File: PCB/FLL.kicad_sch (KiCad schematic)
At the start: 10 parts, among them J1 Jack-DC, U1 MCP73831-2-MC, U3 LM317L_SOT-89

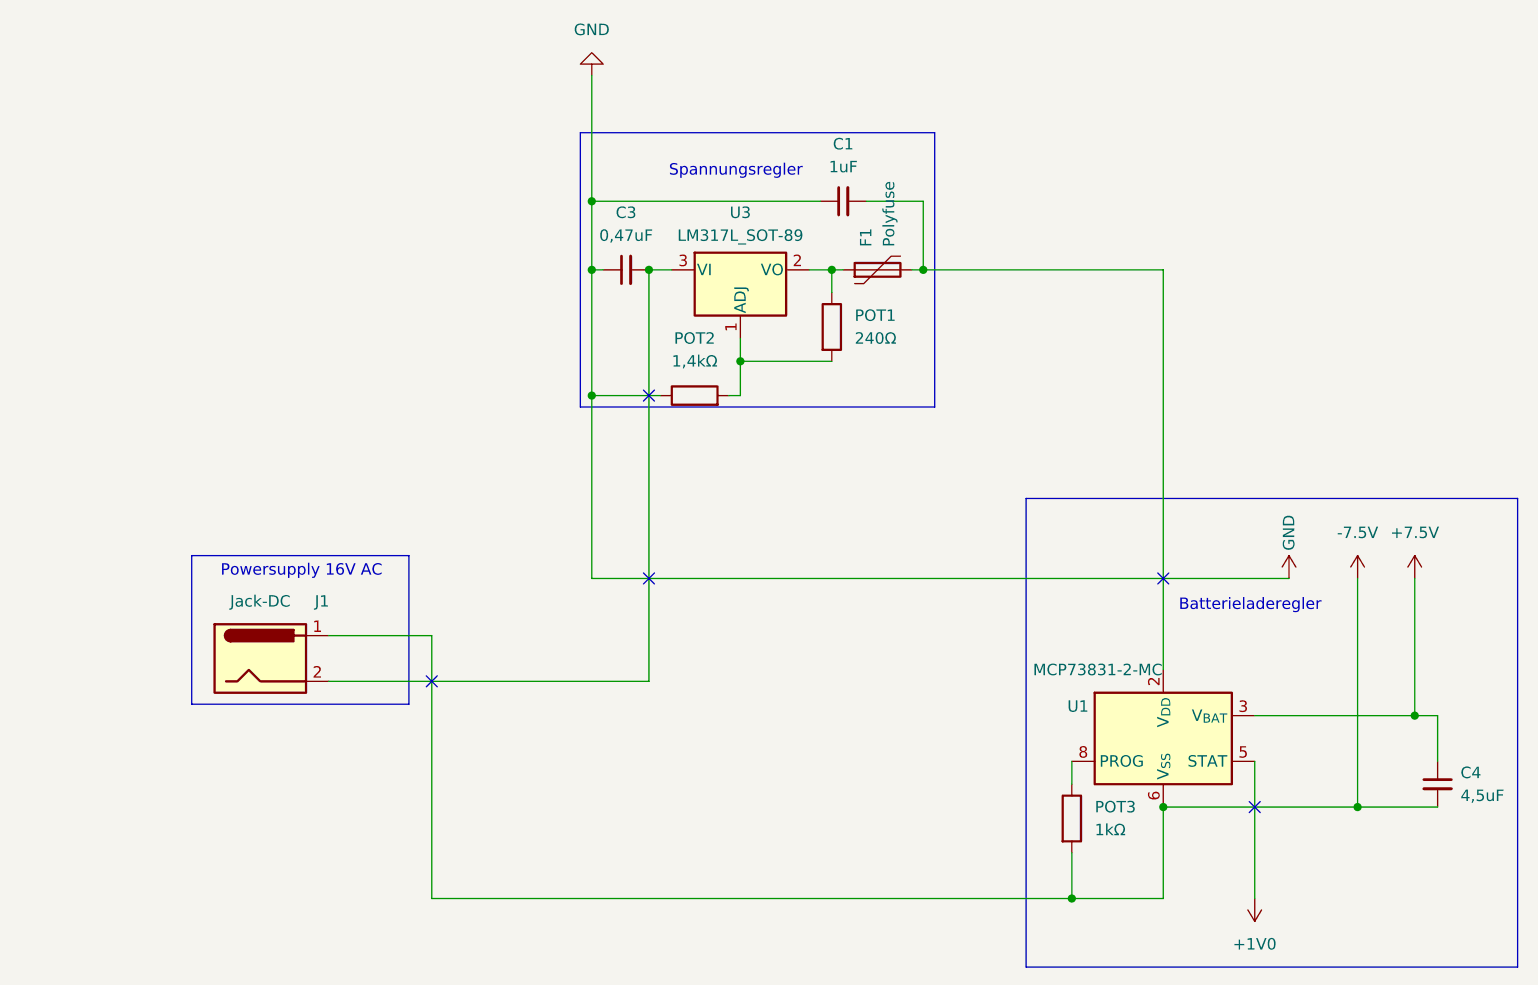
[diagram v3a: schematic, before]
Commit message: Update PCB design configuration and remove unnecessary files
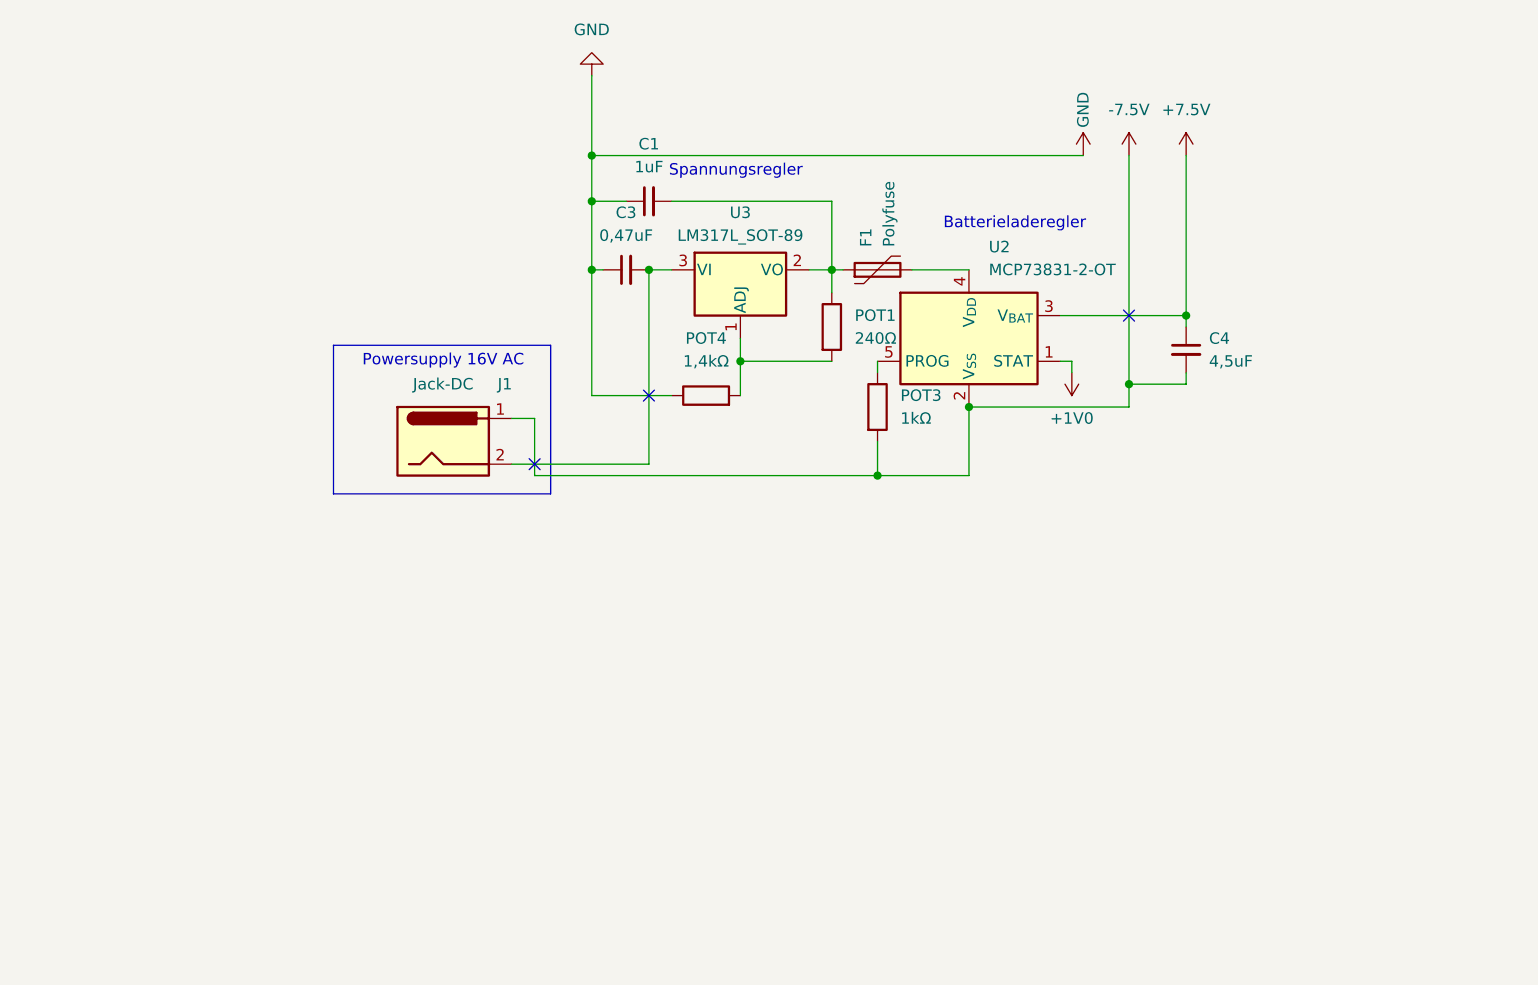
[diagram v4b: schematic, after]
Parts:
- removed POT2: 1,4kΩ, Resistor_SMD:R_0603_1608Metric_Pad0.98x0.95mm_HandSolder, symbol Device:R
- removed U1: MCP73831-2-MC, Package_DFN_QFN:DFN-8-1EP_3x2mm_P0.5mm_EP1.7x1.4mm, symbol Battery_Management:MCP73831-2-MC
- added POT4: 1,4kΩ, Resistor_SMD:R_0603_1608Metric_Pad0.98x0.95mm_HandSolder, symbol Device:R
- added U2: MCP73831-2-OT, Package_TO_SOT_SMD:SOT-23-5, symbol Battery_Management:MCP73831-2-OT
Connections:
- net +1V0: now also U2.1 (STAT)
- net +7.5V: now also U2.3 (V_{BAT})
- net -7.5V: now also U2.2 (V_{SS})
- net GND: now also POT4.1
- net at F1.1, POT1.1, U3.2 (VO): now also C1.2
- net at F1.2: now also U2.4 (V_{DD}); no longer C1.2
- net at POT1.2, U3.1 (ADJ): now also POT4.2
- net at POT3.1: now also U2.5 (PROG)
- no-connect marks 5 -> 3
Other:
- moved on the sheet: C1, C4, J1, POT3

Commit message: Added Mouser Electronics Parts
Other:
- title: Large Hub Battery LEGO: 45610 | Charger -> LEGO® Technic (TM) Large Hub Battery: 45610 | Charger
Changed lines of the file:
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@@
 	(paper "A4")
 	(title_block
-		(title "Large Hub Battery LEGO: 45610 | Charger")
+		(title "LEGO® Technic (TM) Large Hub Battery: 45610 | Charger")
 		(date "04.07.2024")
 		(rev "AIIrondev")

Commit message: chore: Remove unused KiCad symbol files
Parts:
- C1: footprint Capacitor_THT:CP_Axial_L10.0mm_D4.5mm_P15.00mm_Horizontal -> C0805C105K4RACTU:C0805
- C3: footprint Capacitor_THT:CP_Axial_L10.0mm_D4.5mm_P15.00mm_Horizontal -> C0805C474K5RACTU:C0805
- C4: value 4,5uF -> 4,7uF; footprint Capacitor_THT:CP_Axial_L10.0mm_D4.5mm_P15.00mm_Horizontal -> C1210C475K4PACTU:C1210
- POT1: value 240Ω -> 1206L05015YR; footprint Resistor_SMD:R_0603_1608Metric_Pad0.98x0.95mm_HandSolder -> 1206L075THYR:1206L05015YR
- POT3, POT4: footprint Resistor_SMD:R_0603_1608Metric_Pad0.98x0.95mm_HandSolder -> ERJ-2RHD1401X:ERJ2RKD1004X
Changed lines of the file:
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@@
 			)
 		)
-		(property "Footprint" "Capacitor_THT:CP_Axial_L10.0mm_D4.5mm_P15.00mm_Horizontal"
+		(property "Footprint" "C0805C474K5RACTU:C0805"
 			(at 119.38 83.82 0)
 			(effects
@@
 			)
 		)
-		(property "Value" "240Ω"
+		(property "Value" "1206L05015YR"
 			(at 144.78 91.4399 0)
 			(effects
@@
 			)
 		)
-		(property "Footprint" "Resistor_SMD:R_0603_1608Metric_Pad0.98x0.95mm_HandSolder"
+		(property "Footprint" "1206L075THYR:1206L05015YR"
 			(at 140.462 90.17 90)
 			(effects
@@
 			)
 		)
-		(property "Footprint" "Resistor_SMD:R_0603_1608Metric_Pad0.98x0.95mm_HandSolder"
+		(property "Footprint" "ERJ-2RHD1401X:ERJ2RKD1004X"
 			(at 145.542 99.06 90)
 			(effects
@@
 			)
 		)
-		(property "Value" "4,5uF"
+		(property "Value" "4,7uF"
 			(at 184.15 93.9862 0)
 			(effects
@@
 			)
 		)
-		(property "Footprint" "Capacitor_THT:CP_Axial_L10.0mm_D4.5mm_P15.00mm_Horizontal"
+		(property "Footprint" "C1210C475K4PACTU:C1210"
 			(at 181.61 92.71 0)
 			(effects
@@
 			)
 		)
-		(property "Footprint" "Resistor_SMD:R_0603_1608Metric_Pad0.98x0.95mm_HandSolder"
+		(property "Footprint" "ERJ-2RHD1401X:ERJ2RKD1004X"
 			(at 128.27 99.568 90)
 			(effects
@@
 			)
 		)
-		(property "Footprint" "Capacitor_THT:CP_Axial_L10.0mm_D4.5mm_P15.00mm_Horizontal"
+		(property "Footprint" "C0805C105K4RACTU:C0805"
 			(at 121.92 76.2 0)
 			(effects

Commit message: chore: Update plot directory for KiCad project
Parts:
- added D1: LED_ARGB, symbol Device:LED_ARGB
- added M1|12V/1A: Fan, symbol Motor:Fan
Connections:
- net -7.5V: now also M1|12V/1A.2 (-)
- net at C3.2, J1.2, U3.3 (VI): now also M1|12V/1A.1 (+)
- net +1V0: no longer names the net of U2.1 (STAT)
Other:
- note added: "Powersupply 12V 2A DC"
- note removed: "Powersupply 16V AC"
- moved on the sheet: J1
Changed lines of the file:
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@@
+	)
+	(junction
+		(at 105.41 105.41)
+		(diameter 0)
+		(color 0 0 0 0)
 	)
 	(junction
@@
 	)
 	(junction
+		(at 105.41 106.68)
+		(diameter 0)
+		(color 0 0 0 0)
+	)
+	(junction
 		(at 181.61 88.9)
 		(diameter 0)
@@
 	)
 	(no_connect
-		(at 109.22 105.41)
-	)
-	(wire
-		(pts
-			(xy 109.22 100.33) (xy 109.22 106.68)
+		(at 97.79 105.41)
+	)
+	(wire
+		(pts
+			(xy 97.79 100.33) (xy 97.79 106.68)
 		)
 		(stroke
@@
 	(wire
 		(pts
-			(xy 106.68 105.41) (xy 121.92 105.41)
+			(xy 95.25 105.41) (xy 105.41 105.41)
 		)
 		(stroke
@@
 	(wire
 		(pts
-			(xy 106.68 100.33) (xy 109.22 100.33)
+			(xy 95.25 100.33) (xy 97.79 100.33)
 		)
 		(stroke
@@
 	(wire
 		(pts
+			(xy 105.41 90.17) (xy 64.77 90.17)
+		)
+		(stroke
+			(width 0)
+			(type default)
+		)
+	)
+	(wire
+		(pts
+			(xy 64.77 111.76) (xy 64.77 105.41)
+		)
+		(stroke
+			(width 0)
+			(type default)
+		)
+	)
+	(wire
+		(pts
 			(xy 157.48 99.06) (xy 175.26 99.06)
 		)
@@
 	(wire
 		(pts
-			(xy 168.91 93.98) (xy 168.91 95.25)
+			(xy 64.77 90.17) (xy 64.77 92.71)
 		)
 		(stroke
@@
 	(wire
 		(pts
+			(xy 105.41 106.68) (xy 147.32 106.68)
+		)
+		(stroke
+			(width 0)
+			(type default)
+		)
+	)
+	(wire
+		(pts
 			(xy 115.57 71.12) (xy 170.18 71.12)
 		)
@@
 	(wire
 		(pts
+			(xy 105.41 106.68) (xy 105.41 111.76)
+		)
+		(stroke
+			(width 0)
+			(type default)
+		)
+	)
+	(wire
+		(pts
 			(xy 175.26 71.12) (xy 175.26 96.52)
 		)
@@
 	(wire
 		(pts
+			(xy 105.41 105.41) (xy 121.92 105.41)
+		)
+		(stroke
+			(width 0)
+			(type default)
+		)
+	)
+	(wire
+		(pts
 			(xy 175.26 96.52) (xy 181.61 96.52)
 		)
@@
 	(wire
 		(pts
-			(xy 109.22 106.68) (xy 147.32 106.68)
+			(xy 97.79 106.68) (xy 105.41 106.68)
 		)
 		(stroke
@@
 	(wire
 		(pts
+			(xy 105.41 111.76) (xy 64.77 111.76)
+		)
+		(stroke
+			(width 0)
+			(type default)
+		)
+	)
+	(wire
+		(pts
 			(xy 147.32 106.68) (xy 157.48 106.68)
 		)
@@
 	(wire
 		(pts
+			(xy 105.41 105.41) (xy 105.41 90.17)
+		)
+		(stroke
+			(width 0)
+			(type default)
+		)
+	)
+	(wire
+		(pts
 			(xy 116.84 83.82) (xy 115.57 83.82)
 		)
@@
 		)
 	)
-	(wire
-		(pts
-			(xy 167.64 93.98) (xy 168.91 93.98)
-		)
-		(stroke
-			(width 0)
-			(type default)
-		)
-	)
 	(rectangle
-		(start 86.868 92.202)
-		(end 110.998 108.712)
+		(start 75.438 92.202)
+		(end 99.568 108.712)
 		(stroke
 			(width 0)
@@
 		)
 	)
-	(text "Powersupply 16V AC"
-		(exclude_from_sim no)
-		(at 99.06 93.98 0)
+	(text "Powersupply 12V 2A DC"
+		(exclude_from_sim no)
+		(at 87.63 93.98 0)
 		(effects
 			(font
@@
 	)
 	(symbol
-		(lib_id "power:+1V0")
-		(at 168.91 95.25 180)
-		(unit 1)
-		(exclude_from_sim no)
-		(in_bom yes)
-		(on_board yes)
-		(dnp no)
-		(fields_autoplaced yes)
-		(property "Reference" "#PWR06"
-			(at 168.91 91.44 0)
-			(effects
-				(font
-					(size 1.27 1.27)
-				)
-				(hide yes)
-			)
-		)
-		(property "Value" "+1V0"
-			(at 168.91 100.33 0)
-			(effects
-				(font
-					(size 1.27 1.27)
-				)
-			)
-		)
-		(property "Footprint" ""
-			(at 168.91 95.25 0)
-			(effects
-				(font
-					(size 1.27 1.27)
-				)
-				(hide yes)
-			)
-		)
-		(property "Datasheet" ""
-			(at 168.91 95.25 0)
-			(effects
-				(font
-					(size 1.27 1.27)
-				)
-				(hide yes)
-			)
-		)
-		(property "Description" "Power symbol creates a global label with name \"+1V0\""
-			(at 168.91 95.25 0)
-			(effects
-				(font
-					(size 1.27 1.27)
-				)
-				(hide yes)
-			)
-		)
-		(pin "1"
-		)
-		(instances
-			(project ""
-				(path "/eebf961a-9e34-427c-a1d5-e0dfc5b48cc6"
-					(reference "#PWR06")
-					(unit 1)
-				)
-			)
-		)
-	)
-	(symbol
 		(lib_id "power:GND")
 		(at 115.57 62.23 180)
@@
 	(symbol
 		(lib_id "Connector:Jack-DC")
-		(at 99.06 102.87 0)
+		(at 87.63 102.87 0)
 		(unit 1)
 		(exclude_from_sim no)
@@
 		(dnp no)
 		(property "Reference" "J1"
-			(at 105.918 96.52 0)
+			(at 94.488 96.52 0)
 			(effects
 				(font
@@
 		)
 		(property "Value" "Jack-DC"
-			(at 99.06 96.52 0)
+			(at 87.63 96.52 0)
 			(effects
 				(font
@@
 		)
 		(property "Footprint" ""
-			(at 100.33 103.886 0)
+			(at 88.9 103.886 0)
 			(effects
 				(font
@@
 		)
 		(property "Datasheet" "~"
-			(at 100.33 103.886 0)
+			(at 88.9 103.886 0)
 			(effects
 				(font
@@
 		)
 		(property "Description" "DC Barrel Jack"
-			(at 99.06 102.87 0)
+			(at 87.63 102.87 0)
 			(effects
 				(font
@@
 					(unit 1)
 				)
+			)
+		)
+	)
+	(symbol
+		(lib_id "Motor:Fan")
+		(at 64.77 100.33 0)
+		(unit 1)
+		(exclude_from_sim no)
+		(in_bom yes)
+		(on_board yes)
+		(dnp no)
+		(property "Reference" "M1|12V/1A"
+			(at 59.182 91.694 0)
+			(effects
+				(font
+					(size 1.27 1.27)
+				)
+				(justify left)
+			)
+		)
+		(property "Value" "Fan"
+			(at 69.85 101.5999 0)
+			(effects
+				(font
+					(size 1.27 1.27)
+				)
+				(justify left)
+			)
+		)
+		(property "Footprint" ""
+			(at 64.77 100.076 0)
+			(effects
+				(font
+					(size 1.27 1.27)
+				)
+				(hide yes)
+			)
+		)
+		(property "Datasheet" "~"
+			(at 64.77 100.076 0)
+			(effects
+				(font
+					(size 1.27 1.27)
+				)
+				(hide yes)
+			)
+		)
+		(property "Description" "Fan"
+			(at 64.77 100.33 0)
+			(effects
+				(font
+					(size 1.27 1.27)
+				)
+				(hide yes)
+			)
+		)
+		(pin "1"
+		)
+		(pin "2"
+		)
+		(instances
+			(project ""
+				(path "/eebf961a-9e34-427c-a1d5-e0dfc5b48cc6"
+					(reference "M1|12V/1A")
+					(unit 1)
+				)
+			)
+		)
+	)
+	(symbol
+		(lib_id "Device:LED_ARGB")
+		(at 167.64 111.76 270)
+		(unit 1)
+		(exclude_from_sim no)
+		(in_bom yes)
+		(on_board yes)
+		(dnp no)
+		(fields_autoplaced yes)
+		(property "Reference" "D1"
+			(at 181.61 111.76 0)
+			(effects
+				(font
+					(size 1.27 1.27)
+				)
+			)
+		)
+		(property "Value" "LED_ARGB"
+			(at 179.07 111.76 0)
+			(effects
+				(font
+					(size 1.27 1.27)
+				)
+			)
+		)
+		(property "Footprint" ""
+			(at 166.37 111.76 0)
+			(effects
+				(font
+					(size 1.27 1.27)
+				)
+				(hide yes)
+			)
+		)
+		(property "Datasheet" "~"
+			(at 166.37 111.76 0)
+			(effects
+				(font
+					(size 1.27 1.27)
+				)
+				(hide yes)
+			)
+		)
+		(property "Description" "RGB LED, anode/red/green/blue"
+			(at 167.64 111.76 0)
+			(effects
+				(font
+					(size 1.27 1.27)
+				)
+				(hide yes)
+			)
+		)
+		(pin "2"
+		)
+		(pin "3"
+		)
+		(pin "4"
+		)
+		(pin "1"
+		)
+		(instances
+			(project ""
+				(path "/eebf961a-9e34-427c-a1d5-e0dfc5b48cc6"
+					(reference "D1")
+					(unit 1)
+				)

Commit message: Rework ALL
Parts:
- POT1: value 1206L05015YR -> 240Ω; footprint 1206L075THYR:1206L05015YR -> ERJ-2RHD1401X:ERJ2RKD1004X
- renumbered M1|12V/1A to M1|12V/1A1
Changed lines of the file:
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@@
+	)
+	(symbol
+		(lib_id "power:+7.5V")
+		(at 181.61 71.12 0)
+		(unit 1)
+		(exclude_from_sim no)
+		(in_bom yes)
+		(on_board yes)
+		(dnp no)
+		(fields_autoplaced yes)
+		(property "Reference" "#PWR02"
+			(at 181.61 74.93 0)
+			(effects
+				(font
+					(size 1.27 1.27)
+				)
+				(hide yes)
+			)
+		)
+		(property "Value" "+7.5V"
+			(at 181.61 66.04 0)
+			(effects
+				(font
+					(size 1.27 1.27)
+				)
+			)
+		)
+		(property "Footprint" ""
+			(at 181.61 71.12 0)
+			(effects
+				(font
+					(size 1.27 1.27)
+				)
+				(hide yes)
+			)
+		)
+		(property "Datasheet" ""
+			(at 181.61 71.12 0)
+			(effects
+				(font
+					(size 1.27 1.27)
+				)
+				(hide yes)
+			)
+		)
+		(property "Description" "Power symbol creates a global label with name \"+7.5V\""
+			(at 181.61 71.12 0)
+			(effects
+				(font
+					(size 1.27 1.27)
+				)
+				(hide yes)
+			)
+		)
+		(pin "1"
+		)
+		(instances
+			(project ""
+				(path "/eebf961a-9e34-427c-a1d5-e0dfc5b48cc6"
+					(reference "#PWR02")
+					(unit 1)
+				)
+			)
+		)
 	)
 	(symbol
@@
 			)
 		)
-		(property "Value" "1206L05015YR"
+		(property "Value" "240Ω"
 			(at 144.78 91.4399 0)
 			(effects
@@
 			)
 		)
-		(property "Footprint" "1206L075THYR:1206L05015YR"
+		(property "Footprint" "ERJ-2RHD1401X:ERJ2RKD1004X "
 			(at 140.462 90.17 90)
 			(effects
@@
 			)
 		)
-		(property "Datasheet" "240Ω"
+		(property "Datasheet" "~"
 			(at 142.24 90.17 0)
 			(effects
@@
 		)
 		(instances
-			(project ""
+			(project "FLL"
 				(path "/eebf961a-9e34-427c-a1d5-e0dfc5b48cc6"
 					(reference "POT1")
-					(unit 1)
-				)
-			)
-		)
-	)
-	(symbol
-		(lib_id "power:+7.5V")
-		(at 181.61 71.12 0)
-		(unit 1)
-		(exclude_from_sim no)
-		(in_bom yes)
-		(on_board yes)
-		(dnp no)
-		(fields_autoplaced yes)
-		(property "Reference" "#PWR02"
-			(at 181.61 74.93 0)
-			(effects
-				(font
-					(size 1.27 1.27)
-				)
-				(hide yes)
-			)
-		)
-		(property "Value" "+7.5V"
-			(at 181.61 66.04 0)
-			(effects
-				(font
-					(size 1.27 1.27)
-				)
-			)
-		)
-		(property "Footprint" ""
-			(at 181.61 71.12 0)
-			(effects
-				(font
-					(size 1.27 1.27)
-				)
-				(hide yes)
-			)
-		)
-		(property "Datasheet" ""
-			(at 181.61 71.12 0)
-			(effects
-				(font
-					(size 1.27 1.27)
-				)
-				(hide yes)
-			)
-		)
-		(property "Description" "Power symbol creates a global label with name \"+7.5V\""
-			(at 181.61 71.12 0)
-			(effects
-				(font
-					(size 1.27 1.27)
-				)
-				(hide yes)
-			)
-		)
-		(pin "1"
-		)
-		(instances
-			(project ""
-				(path "/eebf961a-9e34-427c-a1d5-e0dfc5b48cc6"
-					(reference "#PWR02")
 					(unit 1)
 				)
@@
 		(on_board yes)
 		(dnp no)
-		(property "Reference" "M1|12V/1A"
+		(property "Reference" "M1|12V/1A1"
 			(at 59.182 91.694 0)
 			(effects
@@
 			(project ""
 				(path "/eebf961a-9e34-427c-a1d5-e0dfc5b48cc6"
-					(reference "M1|12V/1A")
-					(unit 1)
-				)
+					(reference "M1|12V/1A1")
+					(unit 1)
+				)
